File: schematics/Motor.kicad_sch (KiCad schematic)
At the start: 9 parts

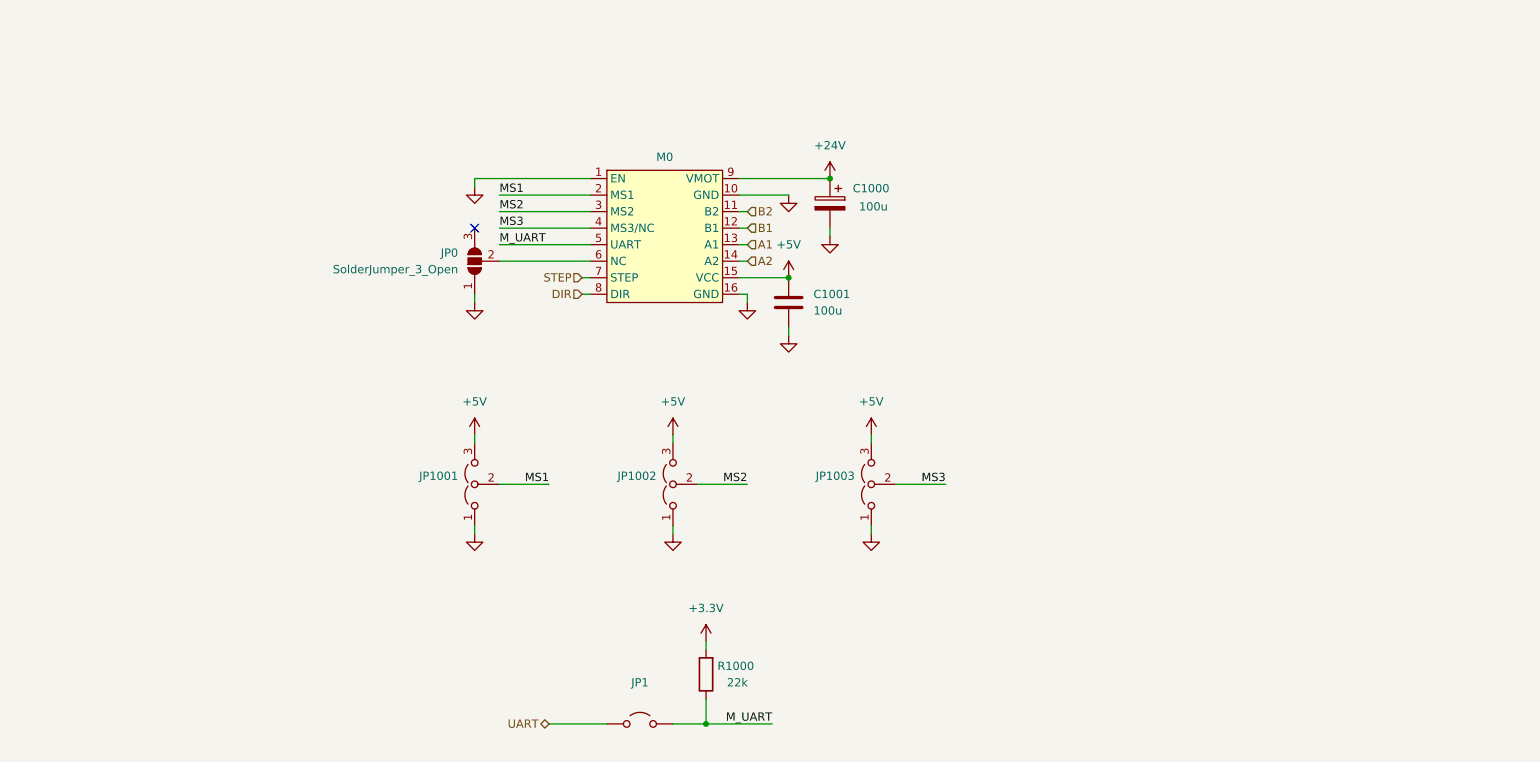
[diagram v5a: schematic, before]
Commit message: Изменил на подключение промышленного мотора
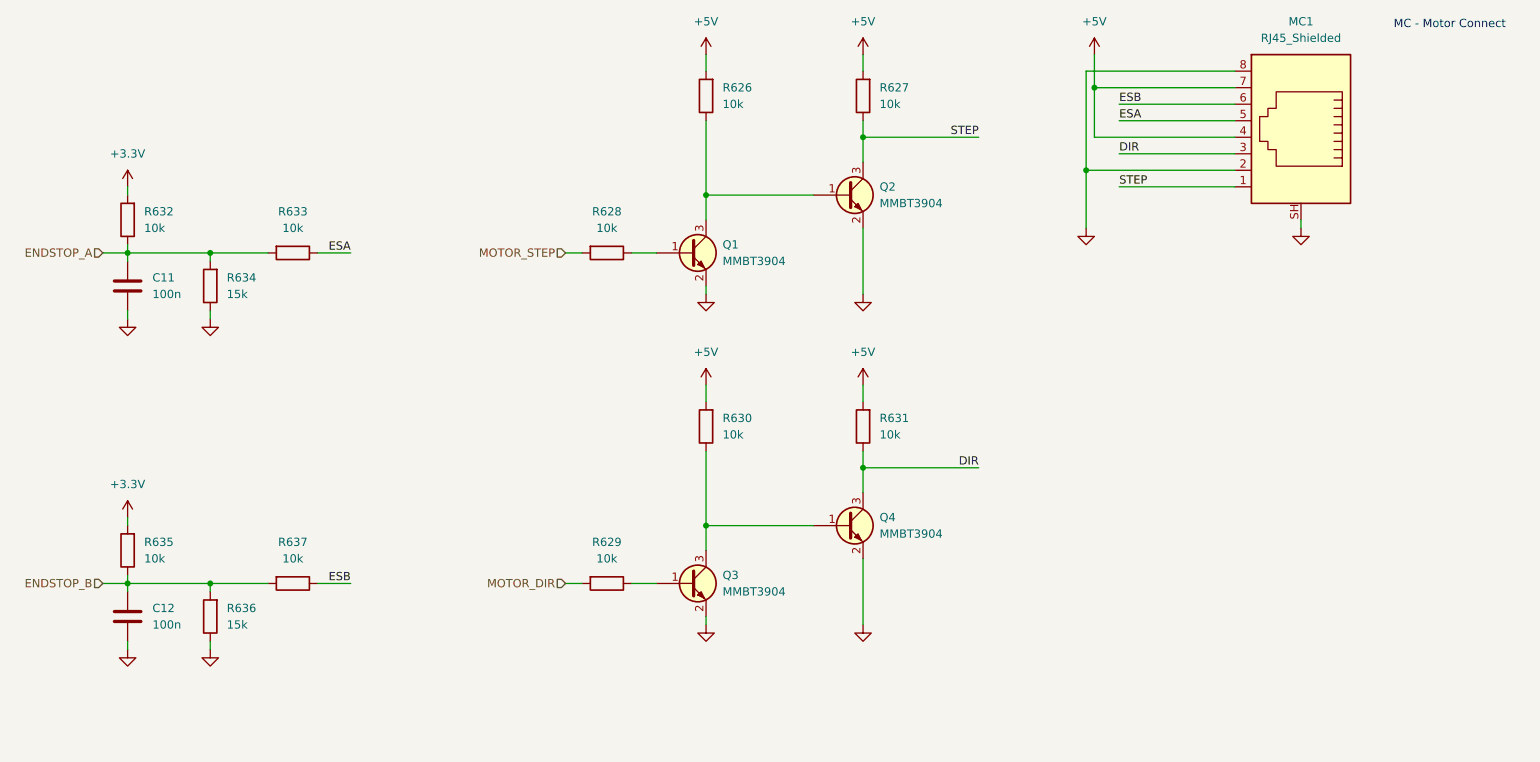
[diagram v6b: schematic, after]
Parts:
- removed C1000: 100u, Capacitor_SMD:CP_Elec_6.3x7.7, symbol Device:C_Polarized
- removed C1001: 100u, Capacitor_SMD:C_0805_2012Metric, symbol Device:C
- removed JP0: SolderJumper_3_Open, Jumper:SolderJumper-3_P1.3mm_Open_RoundedPad1.0x1.5mm, symbol Jumper:SolderJumper_3_Open
- removed JP1: ~, Connector_PinHeader_2.54mm:PinHeader_1x02_P2.54mm_Vertical, symbol Jumper:Jumper_2_Open
- removed JP1001, JP1002, JP1003: ~, Connector_PinHeader_2.54mm:PinHeader_1x03_P2.54mm_Vertical, symbol Jumper:Jumper_3_Open
- removed M0: ~, Library:MotorSocket, symbol New_Library:TMCxxxx
- removed R1000: 22k, Resistor_SMD:R_0805_2012Metric, symbol Device:R
- added C11, C12: 100n, Capacitor_SMD:C_0805_2012Metric, symbol Device:C
- added MC1: RJ45_Shielded, Connector_RJ:RJ45_Ninigi_GE, symbol Connector:RJ45_Shielded
- added Q1, Q2, Q3, Q4: MMBT3904, PCM_4ms_Package_SOT:SOT-23, symbol PCM_Transistor_BJT_AKL:MMBT3904
- added R626, R627, R628, R629, R630, R631, R632, R633, R635, R637: 10k, Resistor_SMD:R_0805_2012Metric, symbol Device:R
- added R634, R636: 15k, Resistor_SMD:R_0805_2012Metric, symbol Device:R
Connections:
- net +3.3V: now also R632.2, R635.2
- net +5V: now also MC1.4, MC1.7, R626.2, R627.2, R630.2, R631.2
- net DIR: now also MC1.3, Q4.3 (C), R631.1
- net GND: now also C11.2, C12.2, MC1.2, MC1.8, MC1.SH, Q1.2 (E), Q2.2 (E), Q3.2 (E), Q4.2 (E), R634.1, R636.1
- net STEP: now also MC1.1, Q2.3 (C), R627.1
- new net: Q1.1 (B), R628.1
- new net: Q1.3 (C), Q2.1 (B), R626.1
- new net: Q3.1 (B), R629.1
- new net: Q3.3 (C), Q4.1 (B), R630.1
- new net ENDSTOP_A: C11.1, R632.1, R633.2, R634.2
- new net ENDSTOP_B: C12.1, R635.1, R636.2, R637.2
- new net ESA: MC1.5, R633.1
- new net ESB: MC1.6, R637.1
- new net MOTOR_DIR: R629.2
- new net MOTOR_STEP: R628.2
- no-connect marks 1 -> 0
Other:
- note added: "MC - Motor Connect"

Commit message: Предфинальный облик мотора, нужно еще добавить пару моментов
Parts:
- renumbered MC1 to MC10, Q1 to Q34

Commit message: Добавил разъемы, для концевиков
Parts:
- added ESA?: ESA, Connector_JST:JST_PH_B3B-PH-K_1x03_P2.00mm_Vertical, symbol Connector:Conn_01x03_Socket
- added ESB?: ESB, Connector_JST:JST_PH_B3B-PH-K_1x03_P2.00mm_Vertical, symbol Connector:Conn_01x03_Socket
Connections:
- net +5V: now also ESA?.1 (Pin_1), ESB?.1 (Pin_1)
- net ESA: now also ESA?.2 (Pin_2)
- net ESB: now also ESB?.2 (Pin_2)
- net GND: now also ESA?.3 (Pin_3), ESB?.3 (Pin_3)
